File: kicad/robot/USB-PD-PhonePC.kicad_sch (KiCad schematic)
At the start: 50 parts, among them J4 USB4120-03-C_REVA, U11 MAX77958EWV+T, U15 ESD122DMYR, U16 fpf1048bucx, U17 TPS61253AYFFR

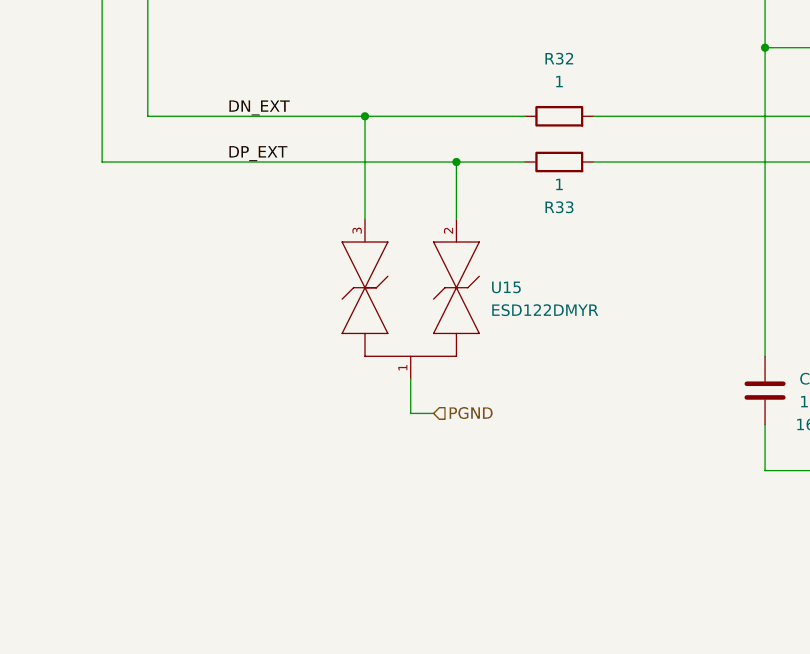
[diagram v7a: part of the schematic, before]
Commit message: Swapped out ESD diodes on DN/DP lines
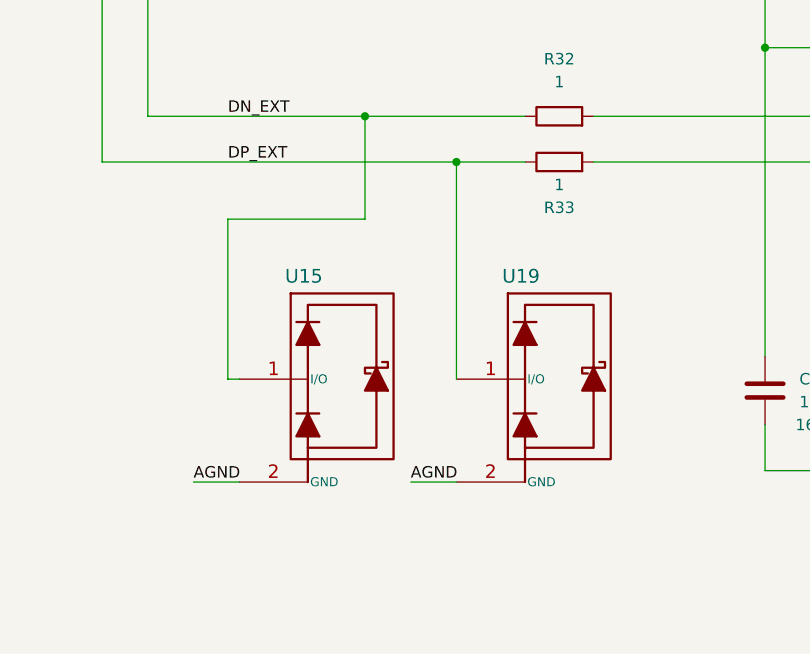
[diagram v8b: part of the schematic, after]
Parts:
- removed U15: ESD122DMYR, Diode_SMD:Texas_Instruments-DMY0003A-0-0-MFG, symbol Diode:ESD122DMYR
- added U15, U19: TPD1E05U06, Package_X1SON:TPD1E05U06DPYR, symbol Diode:TPD1E05U06
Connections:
- net AGND: now also U15.2 (GND), U19.2 (GND)
- net DN_EXT: now also U15.1 (I/O)
- net DP_EXT: now also U19.1 (I/O)
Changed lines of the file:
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@@
+    (stroke (width 0) (type default) (color 0 0 0 0))
+  )
+  (wire (pts (xy 160.02 240.03) (xy 160.02 257.81))
     (stroke (width 0) (type default) (color 0 0 0 0))
   )
@@
     (stroke (width 0) (type default) (color 0 0 0 0))
   )
+  (wire (pts (xy 175.26 240.03) (xy 160.02 240.03))
+    (stroke (width 0) (type default) (color 0 0 0 0))
+  )
   (wire (pts (xy 219.71 262.89) (xy 219.71 267.97))
     (stroke (width 0) (type default) (color 0 0 0 0))
@@
     (stroke (width 0) (type default) (color 0 0 0 0))
   )
-  (wire (pts (xy 182.88 261.62) (xy 180.34 261.62))
-    (stroke (width 0) (type default) (color 0 0 0 0))
-  )
   (wire (pts (xy 410.21 120.65) (xy 416.56 120.65))
     (stroke (width 0) (type default) (color 0 0 0 0))
@@
     (stroke (width 0) (type default) (color 0 0 0 0))
   )
+  (wire (pts (xy 156.21 269.24) (xy 161.29 269.24))
+    (stroke (width 0) (type default) (color 0 0 0 0))
+  )
   (wire (pts (xy 92.71 132.08) (xy 128.27 132.08))
     (stroke (width 0) (type default) (color 0 0 0 0))
@@
     (stroke (width 0) (type default) (color 0 0 0 0))
   )
+  (wire (pts (xy 160.02 257.81) (xy 161.29 257.81))
+    (stroke (width 0) (type default) (color 0 0 0 0))
+  )
   (polyline (pts (xy 412.75 284.48) (xy 457.2 284.48))
     (stroke (width 0) (type default) (color 0 0 0 0))
@@
     (stroke (width 0) (type default) (color 0 0 0 0))
   )
-  (wire (pts (xy 180.34 261.62) (xy 180.34 257.81))
-    (stroke (width 0) (type default) (color 0 0 0 0))
-  )
   (wire (pts (xy 92.71 165.1) (xy 92.71 162.56))
     (stroke (width 0) (type default) (color 0 0 0 0))
@@
     (stroke (width 0) (type default) (color 0 0 0 0))
   )
-  (wire (pts (xy 185.42 233.68) (xy 185.42 240.03))
+  (wire (pts (xy 185.42 233.68) (xy 185.42 257.81))
     (stroke (width 0) (type default) (color 0 0 0 0))
   )
@@
   )
   (wire (pts (xy 82.55 201.93) (xy 92.71 201.93))
+    (stroke (width 0) (type default) (color 0 0 0 0))
+  )
+  (wire (pts (xy 180.34 269.24) (xy 185.42 269.24))
     (stroke (width 0) (type default) (color 0 0 0 0))
   )
@@
     (effects (font (size 1.27 1.27)) (justify left bottom))
   )
+  (label "AGND" (at 180.34 269.24 0)
+    (effects (font (size 1.27 1.27)) (justify left bottom))
+  )
   (label "GPIO1" (at 82.55 201.93 0)
     (effects (font (size 1.27 1.27)) (justify left bottom))
@@
     (effects (font (size 1.27 1.27)) (justify right bottom))
   )
+  (label "AGND" (at 156.21 269.24 0)
+    (effects (font (size 1.27 1.27)) (justify left bottom))
+  )
   (hierarchical_label "VIO2" (shape input) (at 321.31 143.51 180)
     (effects (font (size 1.27 1.27)) (justify right))
@@
   (hierarchical_label "PGND" (shape input) (at 162.56 143.51 270)
     (effects (font (size 1.27 1.27)) (justify right))
-  )
-  (hierarchical_label "PGND" (shape input) (at 182.88 261.62 0)
-    (effects (font (size 1.27 1.27)) (justify left))
   )
   (hierarchical_label "VIO2" (shape input) (at 375.92 246.38 0)
@@
     (pin "2")
   )
+  (symbol (lib_id "Diode:TPD1E05U06") (at 172.72 257.81 0) (unit 1)
+    (in_bom yes) (on_board yes)
+    (property "Reference" "U15" (id 0) (at 166.37 246.38 0)
+      (effects (font (size 1.524 1.524)) (justify left))
+    )
+    (property "Value" "TPD1E05U06" (id 1) (at 172.72 276.86 0)
+      (effects (font (size 1.524 1.524)) hide)
+    )
+    (property "Footprint" "Package_X1SON:TPD1E05U06DPYR" (id 2) (at 172.72 274.32 0)
+      (effects (font (size 1.524 1.524)) hide)
+    )
+    (property "Datasheet" "https://www.ti.com/lit/gpn/tpd1e05u06" (id 3) (at 173.355 271.145 0)
+      (effects (font (size 1.524 1.524)) hide)
+    )
+    (pin "1")
+    (pin "2")
+  )
   (symbol (lib_id "Device:R") (at 334.01 229.87 0) (unit 1)
     (in_bom yes) (on_board yes) (fields_autoplaced)
@@
     (pin "1")
     (pin "2")
-  )
-  (symbol (lib_id "Diode:ESD122DMYR") (at 185.42 237.49 270) (unit 1)
-    (in_bom yes) (on_board yes) (fields_autoplaced)
-    (property "Reference" "U15" (id 0) (at 189.23 247.6499 90)
-      (effects (font (size 1.27 1.27)) (justify left))
-    )
-    (property "Value" "ESD122DMYR" (id 1) (at 189.23 250.1899 90)
-      (effects (font (size 1.27 1.27)) (justify left))
-    )
-    (property "Footprint" "Diode_SMD:Texas_Instruments-DMY0003A-0-0-MFG" (id 2) (at 195.58 237.49 0)
-      (effects (font (size 1.27 1.27)) (justify left) hide)
-    )
-    (property "Datasheet" "https://www.ti.com/lit/gpn/esd122" (id 3) (at 198.12 237.49 0)
-      (effects (font (size 1.27 1.27)) (justify left) hide)
-    )
-    (property "ambient temperature range high" "+125°C" (id 4) (at 200.66 237.49 0)
-      (effects (font (size 1.27 1.27)) (justify left) hide)
-    )
-    (property "ambient temperature range low" "-40°C" (id 5) (at 203.2 237.49 0)
-      (effects (font (size 1.27 1.27)) (justify left) hide)
-    )
-    (property "automotive" "No" (id 6) (at 205.74 237.49 0)
-      (effects (font (size 1.27 1.27)) (justify left) hide)
-    )
-    (property "breakdown voltage" "5.1V" (id 7) (at 208.28 237.49 0)
-      (effects (font (size 1.27 1.27)) (justify left) hide)
-    )
-    (property "capacitance" "0.2pF" (id 8) (at 210.82 237.49 0)
-      (effects (font (size 1.27 1.27)) (justify left) hide)
-    )
-    (property "category" "IC" (id 9) (at 213.36 237.49 0)
-      (effects (font (size 1.27 1.27)) (justify left) hide)
-    )
-    (property "clamping voltage" "8.4V" (id 10) (at 215.9 237.49 0)
-      (effects (font (size 1.27 1.27)) (justify left) hide)
-    )
-    (property "device class L1" "Circuit Protection" (id 11) (at 218.44 237.49 0)
-      (effects (font (size 1.27 1.27)) (justify left) hide)
-    )
-    (property "device class L2" "ESD and Circuit Protection ICs" (id 12) (at 220.98 237.49 0)
-      (effects (font (size 1.27 1.27)) (justify left) hide)
-    )
-    (property "device class L3" "unset" (id 13) (at 223.52 237.49 0)
-      (effects (font (size 1.27 1.27)) (justify left) hide)
-    )
-    (property "digikey description" "TVS DIODE 3.6V 8.4V 3X2SON" (id 14) (at 226.06 237.49 0)
-      (effects (font (size 1.27 1.27)) (justify left) hide)
-    )
-    (property "digikey part number" "296-47120-1-ND" (id 15) (at 228.6 237.49 0)
-      (effects (font (size 1.27 1.27)) (justify left) hide)
-    )
-    (property "direction" "Bidirectional" (id 16) (at 231.14 237.49 0)
-      (effects (font (size 1.27 1.27)) (justify left) hide)
-    )
-    (property "height" "0.4mm" (id 17) (at 233.68 237.49 0)
-      (effects (font (size 1.27 1.27)) (justify left) hide)
-    )
-    (property "interface" "USB" (id 18) (at 236.22 237.49 0)
-      (effects (font (size 1.27 1.27)) (justify left) hide)
-    )
-    (property "lead free" "Yes" (id 19) (at 238.76 237.49 0)
-      (effects (font (size 1.27 1.27)) (justify left) hide)
-    )
-    (property "library id" "f275e4f2fb3d1a8f" (id 20) (at 241.3 237.49 0)
-      (effects (font (size 1.27 1.27)) (justify left) hide)
-    )
-    (property "manufacturer" "" (id 21) (at 243.84 237.49 0)
-      (effects (font (size 1.27 1.27)) (justify left) hide)
-    )
-    (property "mouser part number" "595-ESD122DMYR" (id 22) (at 246.38 237.49 0)
-      (effects (font (size 1.27 1.27)) (justify left) hide)
-    )
-    (property "number of channels" "2" (id 23) (at 248.92 237.49 0)
-      (effects (font (size 1.27 1.27)) (justify left) hide)
-    )
-    (property "operating supply voltage" "3.6V" (id 24) (at 251.46 237.49 0)
-      (effects (font (size 1.27 1.27)) (justify left) hide)
-    )
-    (property "package" "X2SON3" (id 25) (at 254 237.49 0)
-      (effects (font (size 1.27 1.27)) (justify left) hide)
-    )
-    (property "peak pulse current" "2.5A" (id 26) (at 256.54 237.49 0)
-      (effects (font (size 1.27 1.27)) (justify left) hide)
-    )
-    (property "reverse standoff voltage" "3.6V" (id 27) (at 259.08 237.49 0)
-      (effects (font (size 1.27 1.27)) (justify left) hide)
-    )
-    (property "rohs" "Yes" (id 28) (at 261.62 237.49 0)
-      (effects (font (size 1.27 1.27)) (justify left) hide)
-    )
-    (property "standoff height" "0mm" (id 29) (at 264.16 237.49 0)
-      (effects (font (size 1.27 1.27)) (justify left) hide)
-    )
-    (property "temperature range high" "+125°C" (id 30) (at 266.7 237.49 0)
-      (effects (font (size 1.27 1.27)) (justify left) hide)
-    )
-    (property "temperature range low" "-40°C" (id 31) (at 269.24 237.49 0)
-      (effects (font (size 1.27 1.27)) (justify left) hide)
-    )
-    (property "Part Number" "ESD122DMYR" (id 32) (at 185.42 237.49 0)
-      (effects (font (size 1.27 1.27)) hide)
-    )
-    (property "Manufacturer" "Texas Instruments" (id 33) (at 185.42 237.49 0)
-      (effects (font (size 1.27 1.27)) hide)
-    )
-    (pin "1")
-    (pin "2")
-    (pin "3")
   )
   (symbol (lib_id "Power_Management:fpf1048bucx") (at 267.97 121.92 0) (mirror y) (unit 1)
@@
     (pin "1")
   )
+  (symbol (lib_name "TPD1E05U06_1") (lib_id "Diode:TPD1E05U06") (at 196.85 257.81 0) (unit 1)
+    (in_bom yes) (on_board yes)
+    (property "Reference" "U19" (id 0) (at 190.5 246.38 0)
+      (effects (font (size 1.524 1.524)) (justify left))
+    )
+    (property "Value" "TPD1E05U06" (id 1) (at 196.85 276.86 0)
+      (effects (font (size 1.524 1.524)) hide)
+    )
+    (property "Footprint" "Package_X1SON:TPD1E05U06DPYR" (id 2) (at 196.85 274.32 0)
+      (effects (font (size 1.524 1.524)) hide)
+    )
+    (property "Datasheet" "https://www.ti.com/lit/gpn/tpd1e05u06" (id 3) (at 197.485 271.145 0)
+      (effects (font (size 1.524 1.524)) hide)
+    )
+    (pin "1")
+    (pin "2")
+  )
   (symbol (lib_id "Device:R") (at 278.13 130.81 0) (unit 1)
